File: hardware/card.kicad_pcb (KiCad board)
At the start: 2 copper layers, 143 x 80 mm, 1 part

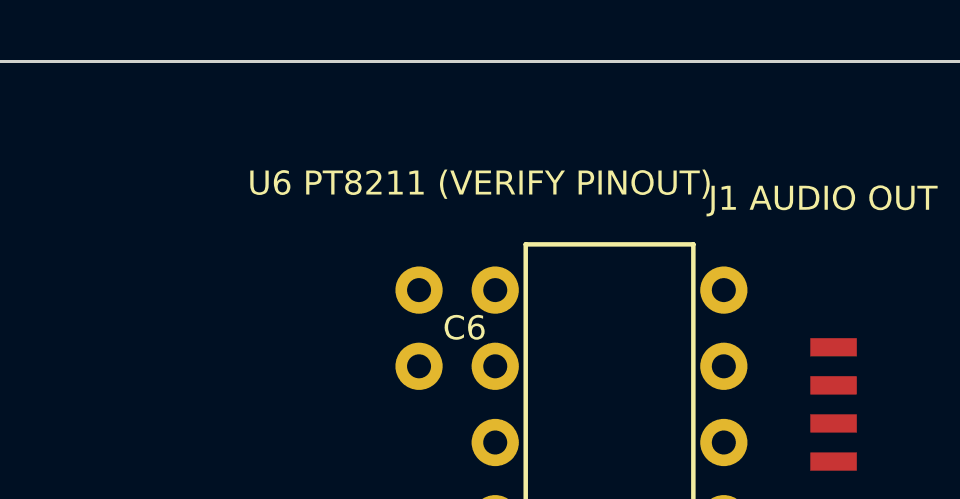
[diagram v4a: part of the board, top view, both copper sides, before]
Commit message: PT8211 datasheet in-tree; pinout verified and corrected
PT8211-S.pdf (Princeton Technology, v1.1) added to hardware/. The
flagged from-memory pinout was right on 6 of 8 pins: 6/8 were L/R
swapped (harmless — both sum to mono) and are now labeled truthfully
(6=LCH, 8=RCH, 7=NC). Datasheet also confirms both packages exist
(PT8211 DIP-8 / PT8211-S SO-8, matching our dual position) and that
the serial format is Japanese/LSB-justified, NOT standard I2S — noted
as a firmware requirement. 3.3V operation noted as Pico-ecosystem
practice vs the 5V nominal. Re-routed, DRC 0/0; fab package
regenerated. The last pre-order human check is closed.

Co-Authored-By: Claude Fable 5 <noreply@anthropic.com>
Claude-Session: https://claude.ai/code/session_01PB6zhL6oFB9zbtD4W85UDt
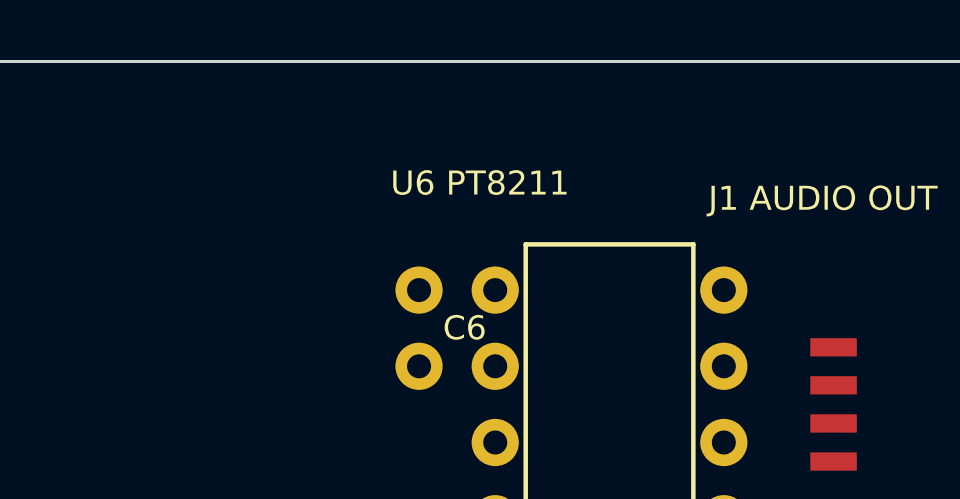
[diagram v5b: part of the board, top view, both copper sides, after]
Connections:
- ? pad 122: AOL -> AOR
- ? pad 126: AOR -> AOL
- ? pad 130: AOL -> AOR
- ? pad 134: AOR -> AOL
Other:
- board text added: "U6 PT8211"
- board text removed: "U6 PT8211 (VERIFY PINOUT)"
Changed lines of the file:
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@@
     (pad "120" thru_hole circle (at 39.37 77.47) (size 1.5748 1.5748) (drill 0.8) (layers "*.Cu" "*.Mask"))
     (pad "121" thru_hole circle (at 102.87 7.62) (size 1.5748 1.5748) (drill 0.8) (layers "*.Cu" "*.Mask") (net 39 "BCK"))
-    (pad "122" thru_hole circle (at 110.49 7.62) (size 1.5748 1.5748) (drill 0.8) (layers "*.Cu" "*.Mask") (net 43 "AOL"))
+    (pad "122" thru_hole circle (at 110.49 7.62) (size 1.5748 1.5748) (drill 0.8) (layers "*.Cu" "*.Mask") (net 44 "AOR"))
     (pad "123" thru_hole circle (at 102.87 10.16) (size 1.5748 1.5748) (drill 0.8) (layers "*.Cu" "*.Mask") (net 40 "WS"))
     (pad "124" thru_hole circle (at 110.49 10.16) (size 1.5748 1.5748) (drill 0.8) (layers "*.Cu" "*.Mask"))
     (pad "125" thru_hole circle (at 102.87 12.7) (size 1.5748 1.5748) (drill 0.8) (layers "*.Cu" "*.Mask") (net 41 "DIN"))
-    (pad "126" thru_hole circle (at 110.49 12.7) (size 1.5748 1.5748) (drill 0.8) (layers "*.Cu" "*.Mask") (net 44 "AOR"))
+    (pad "126" thru_hole circle (at 110.49 12.7) (size 1.5748 1.5748) (drill 0.8) (layers "*.Cu" "*.Mask") (net 43 "AOL"))
     (pad "127" thru_hole circle (at 102.87 15.24) (size 1.5748 1.5748) (drill 0.8) (layers "*.Cu" "*.Mask") (net 1 "GND"))
     (pad "128" thru_hole circle (at 110.49 15.24) (size 1.5748 1.5748) (drill 0.8) (layers "*.Cu" "*.Mask") (net 3 "+3V3"))
     (pad "129" smd rect (at 114.1476 9.525) (size 1.5494 0.6096) (layers "F.Cu" "F.Mask" "F.Paste") (net 39 "BCK"))
-    (pad "130" smd rect (at 119.5324 9.525) (size 1.5494 0.6096) (layers "F.Cu" "F.Mask" "F.Paste") (net 43 "AOL"))
+    (pad "130" smd rect (at 119.5324 9.525) (size 1.5494 0.6096) (layers "F.Cu" "F.Mask" "F.Paste") (net 44 "AOR"))
     (pad "131" smd rect (at 114.1476 10.795) (size 1.5494 0.6096) (layers "F.Cu" "F.Mask" "F.Paste") (net 40 "WS"))
     (pad "132" smd rect (at 119.5324 10.795) (size 1.5494 0.6096) (layers "F.Cu" "F.Mask" "F.Paste"))
     (pad "133" smd rect (at 114.1476 12.065) (size 1.5494 0.6096) (layers "F.Cu" "F.Mask" "F.Paste") (net 41 "DIN"))
-    (pad "134" smd rect (at 119.5324 12.065) (size 1.5494 0.6096) (layers "F.Cu" "F.Mask" "F.Paste") (net 44 "AOR"))
+    (pad "134" smd rect (at 119.5324 12.065) (size 1.5494 0.6096) (layers "F.Cu" "F.Mask" "F.Paste") (net 43 "AOL"))
     (pad "135" smd rect (at 114.1476 13.335) (size 1.5494 0.6096) (layers "F.Cu" "F.Mask" "F.Paste") (net 1 "GND"))
     (pad "136" smd rect (at 119.5324 13.335) (size 1.5494 0.6096) (layers "F.Cu" "F.Mask" "F.Paste") (net 3 "+3V3"))
@@
   (gr_text "U5 HCT138" (at 31.242 56.134) (layer "F.SilkS") (effects (font (size 0.8 0.8) (thickness 0.15))))
   (gr_rect (start 103.886 6.096) (end 109.474 16.764) (layer "F.SilkS") (width 0.15) (fill none))
-  (gr_text "U6 PT8211 (VERIFY PINOUT)" (at 102.362 4.064) (layer "F.SilkS") (effects (font (size 0.8 0.8) (thickness 0.15))))
+  (gr_text "U6 PT8211" (at 102.362 4.064) (layer "F.SilkS") (effects (font (size 0.8 0.8) (thickness 0.15))))
   (gr_text "U6B SOP-8 alt" (at 112.268 15.748) (layer "F.SilkS") (effects (font (size 0.8 0.8) (thickness 0.15))))
   (gr_rect (start 47.752 29.718) (end 99.568 50.546) (layer "F.SilkS") (width 0.15) (fill none))

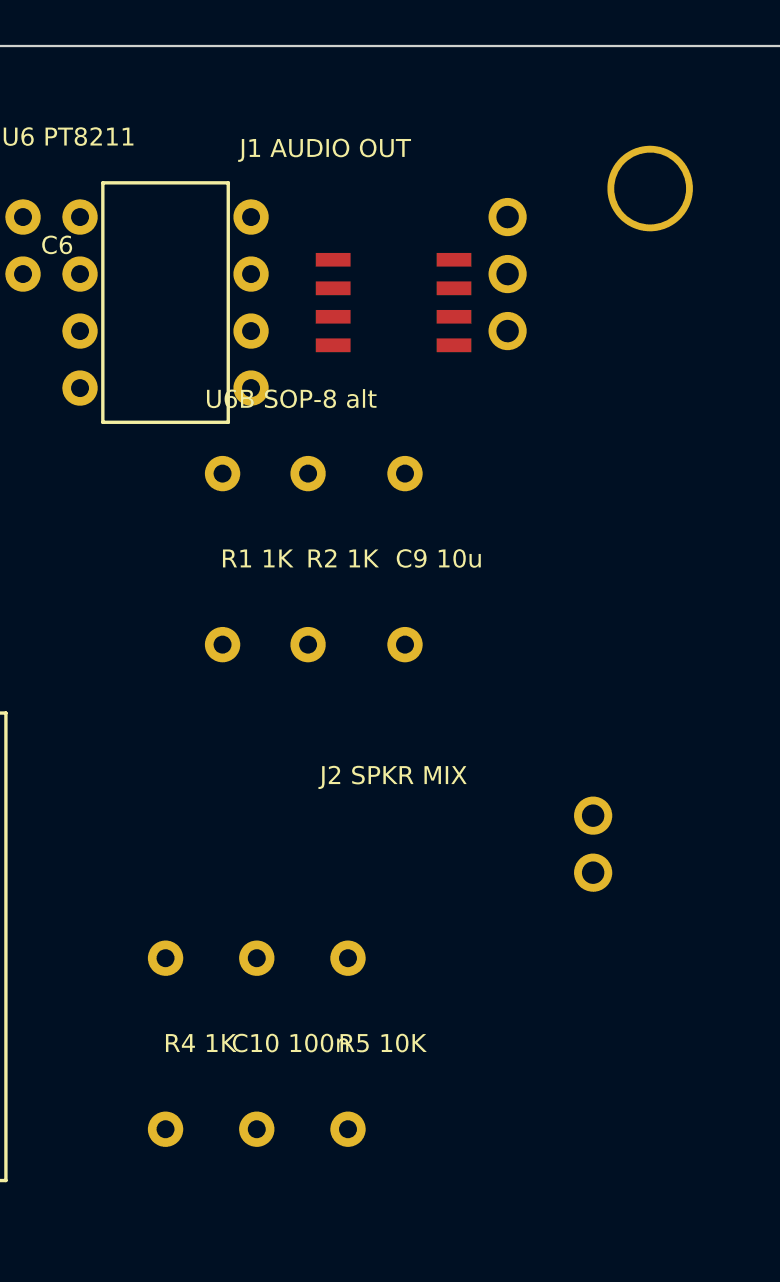
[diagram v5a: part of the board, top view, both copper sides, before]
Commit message: On-board 3.5mm jack, stereo output per the PJRC PT8211 topology
Adopted the protosupplies/PJRC PT8211 adapter design: LCH/RCH each
through 47uF coupling to a real CUI SJ1-3523N TRS jack (footprint
taken from the KiCad-maintained library, rotated so the barrel
overhangs the right board edge) — true stereo replaces the mono sum,
so firmware can pan voices. VDD gets the datasheet's 10R + 47u + 100n
filter (new VDDF rail). PWM fallback and J2 mix-in re-plumbed to the
left channel. Fixed import_ses.py dropping wires for quoted net names
(underscored nets like AOL_C). Re-routed, DRC 0/0, fab package and
docs regenerated.

Co-Authored-By: Claude Fable 5 <noreply@anthropic.com>
Claude-Session: https://claude.ai/code/session_01PB6zhL6oFB9zbtD4W85UDt
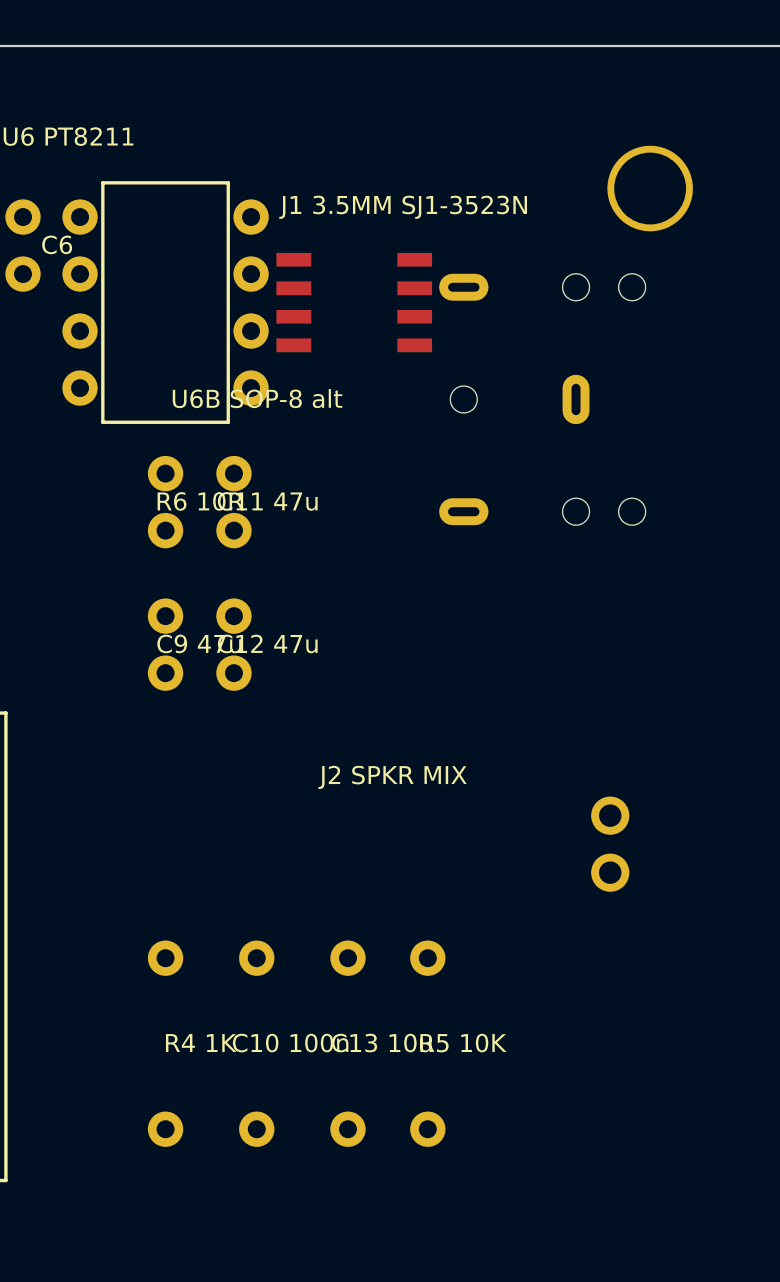
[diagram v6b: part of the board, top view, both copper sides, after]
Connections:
- ? pad 122: AOR -> RCH
- ? pad 126: AOL -> LCH
- ? pad 128: +3V3 -> VDDF
- ? pad 130: AOR -> RCH
- ? pad 134: AOL -> LCH
- ? pad 136: +3V3 -> VDDF
- ? pad 177: AOL -> +3V3
- ? pad 178: ASUM -> VDDF
- ? pad 179: AOR -> VDDF
- ? pad 180: ASUM -> GND
- ? pad 181: ASUM -> LCH
- ? pad 182: AOUT -> AOL_C
- ? pad 183: PWM -> RCH
- ? pad 184: PWMF -> AOR_C
- ? pad 185: PWMF -> PWM
- ? pad 186: GND -> PWMF
- ? pad 188: ASUM -> GND
- ? pad 189: AOUT -> PWMF
- ? pad 190: AOUT -> AOL_C
- ? pad 191: GND -> AOL_C
- ? pad 192: AOUT -> J2SIG
- ? pad 193: GND -> (no net)
- ? pad 194: +3V3 -> (no net)
- ? pad 195: GND -> (no net)
- ? pad 196: +3V3 -> (no net)
- ? pad 197: GND -> (no net)
- ? pad 198: +5V -> J2SIG
- ? pad 200: +5V -> +3V3
- ? pad 202: +5V -> +3V3
- ? pad 204: +3V3 -> +5V
- ? pad 210: (no net) -> VDDF
- ? pad 211: (no net) -> GND
- ? pad 212: (no net) -> +5V
- ? pad 213: (no net) -> GND
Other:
- board text added: "C11 47u"
- board text added: "C12 47u"
- board text added: "C13 10u"
- board text added: "C9 47u"
- board text added: "J1 3.5MM SJ1-3523N"
- board text added: "R6 10R"
- board text removed: "C9 10u"
- board text removed: "J1 AUDIO OUT"
- board text removed: "R1 1K"
- board text removed: "R2 1K"
